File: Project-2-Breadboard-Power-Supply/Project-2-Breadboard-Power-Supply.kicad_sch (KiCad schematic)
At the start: 17 parts, among them J1 Conn_01x02_Pin, J2 Conn_01x02_Pin, J3 Conn_01x03_Pin, J4 Conn_01x03_Pin, J5 Screw_Terminal_01x02, J6 Barrel_Jack_Switch, J7 Screw_Terminal_01x02, U1 LM7805_TO220, U2 LM317_TO-220

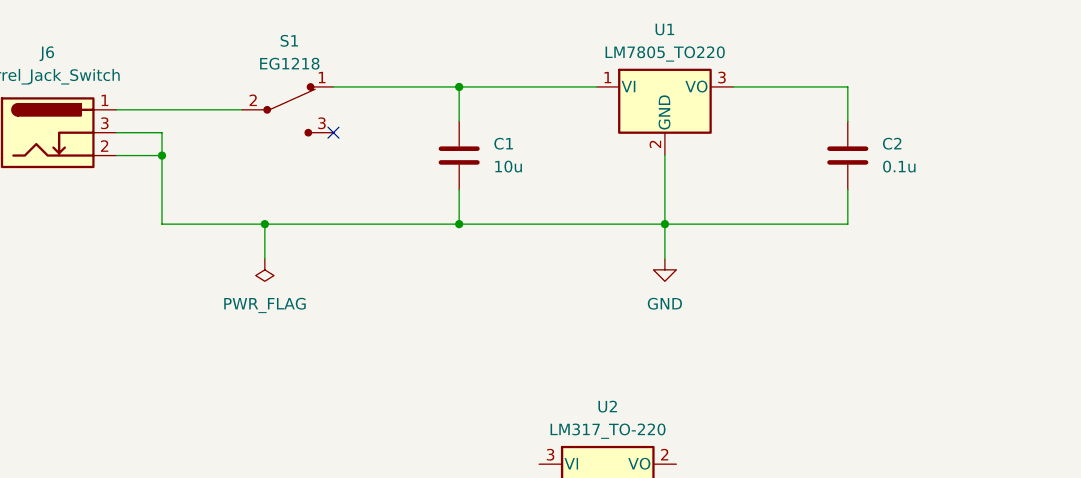
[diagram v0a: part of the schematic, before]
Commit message: add net names (step 5) for sub-net
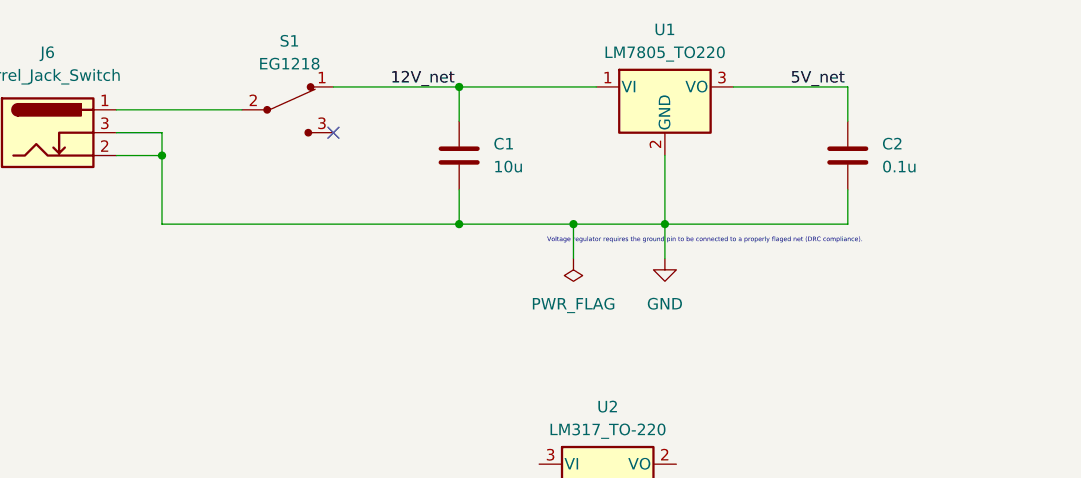
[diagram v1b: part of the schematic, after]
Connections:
- net 12V_net: now reaches C1.1, S1.1, U1.1 (VI)
- net 5V_net: now reaches C2.1, U1.3 (VO)
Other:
- note added: "Voltage regulator requires the ground pin to be connected to a properly flaged net (DRC compliance)."
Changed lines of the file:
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@@
 		(company "jupitersw.com")
+	)
+	(text "Voltage regulator requires the ground pin to be connected to a properly flaged net (DRC compliance)."
+		(exclude_from_sim no)
+		(at 111.125 52.705 0)
+		(effects
+			(font
+				(size 0.5 0.5)
+			)
+		)
 	)
 	(junction
@@
 	)
 	(junction
-		(at 62.23 50.8)
-		(diameter 0)
-		(color 0 0 0 0)
-	)
-	(junction
 		(at 83.82 35.56)
 		(diameter 0)
@@
 		(color 0 0 0 0)
 	)
+	(junction
+		(at 96.52 50.8)
+		(diameter 0)
+		(color 0 0 0 0)
+	)
 	(no_connect
 		(at 69.85 40.64)
@@
 	(wire
 		(pts
-			(xy 62.23 50.8) (xy 83.82 50.8)
-		)
-		(stroke
-			(width 0)
-			(type default)
-		)
-	)
-	(wire
-		(pts
 			(xy 45.72 43.18) (xy 50.8 43.18)
 		)
@@
 	(wire
 		(pts
-			(xy 62.23 50.8) (xy 62.23 54.61)
+			(xy 96.52 50.8) (xy 96.52 54.61)
 		)
 		(stroke
@@
 	(wire
 		(pts
-			(xy 50.8 50.8) (xy 62.23 50.8)
+			(xy 50.8 50.8) (xy 96.52 50.8)
 		)
 		(stroke
@@
 	(wire
 		(pts
-			(xy 83.82 50.8) (xy 106.68 50.8)
-		)
-		(stroke
-			(width 0)
-			(type default)
-		)
-	)
-	(wire
-		(pts
 			(xy 83.82 35.56) (xy 99.06 35.56)
 		)
@@
 	(wire
 		(pts
+			(xy 96.52 50.8) (xy 106.68 50.8)
+		)
+		(stroke
+			(width 0)
+			(type default)
+		)
+	)
+	(wire
+		(pts
 			(xy 50.8 40.64) (xy 50.8 43.18)
 		)
@@
 			(width 0)
 			(type default)
+		)
+	)
+	(label "5V_net"
+		(at 120.65 35.56 0)
+		(effects
+			(font
+				(size 1.27 1.27)
+			)
+			(justify left bottom)
+		)
+	)
+	(label "12V_net"
+		(at 76.2 35.56 0)
+		(effects
+			(font
+				(size 1.27 1.27)
+			)
+			(justify left bottom)
 		)
 	)
@@
 	(symbol
 		(lib_id "power:PWR_FLAG")
-		(at 62.23 54.61 180)
+		(at 96.52 54.61 180)
 		(unit 1)
 		(body_style 1)
@@
 		(fields_autoplaced yes)
 		(property "Reference" "#FLG01"
-			(at 62.23 56.515 0)
+			(at 96.52 56.515 0)
 			(hide yes)
 			(show_name no)
@@
 		)
 		(property "Value" "PWR_FLAG"
-			(at 62.23 59.69 0)
+			(at 96.52 59.69 0)
 			(show_name no)
 			(do_not_autoplace no)
@@
 		)
 		(property "Footprint" ""
-			(at 62.23 54.61 0)
+			(at 96.52 54.61 0)
 			(hide yes)
 			(show_name no)
@@
 		)
 		(property "Datasheet" ""
-			(at 62.23 54.61 0)
+			(at 96.52 54.61 0)
 			(hide yes)
 			(show_name no)
@@
 		)
 		(property "Description" "Special symbol for telling ERC where power comes from"
-			(at 62.23 54.61 0)
-			(hide yes)
-			(show_name no)
+			(at 96.52 54.61 0)
+			(hide yes)
+			(show_name no)

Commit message: add wiring, power flag, net labels to sub-circuit 2 (step 4, 5)
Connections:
- net 12V_net: now also R1.2, U2.3 (VI)
- net GND: now also C3.2, D1.1 (K), R3.1
- net at U2.1 (ADJ): now also R2.1, R3.2
- net 3.3V_net: now reaches U2.2 (VO)
- net 3.3V_net: now also C3.1, R2.2
- net at R1.1: now also D1.2 (A)
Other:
- moved on the sheet: D1, R1, R2, R3

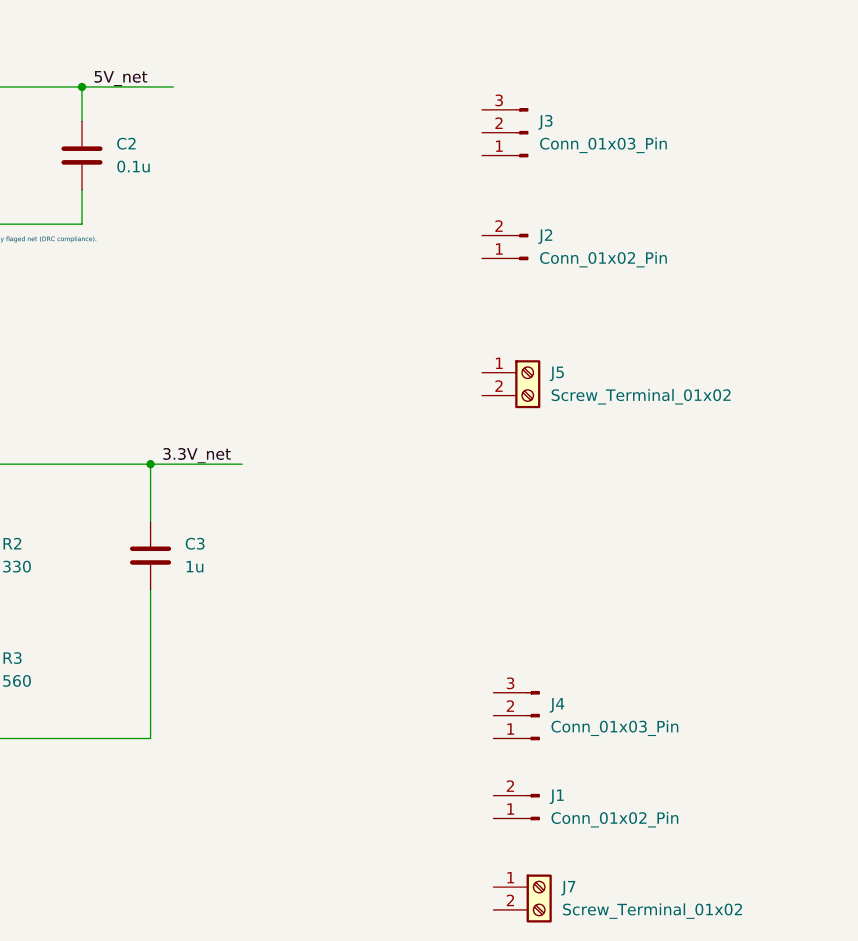
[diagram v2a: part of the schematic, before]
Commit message: add wiring, power flag, net labels to sub-circuits 3, 4 (step 4, 5)
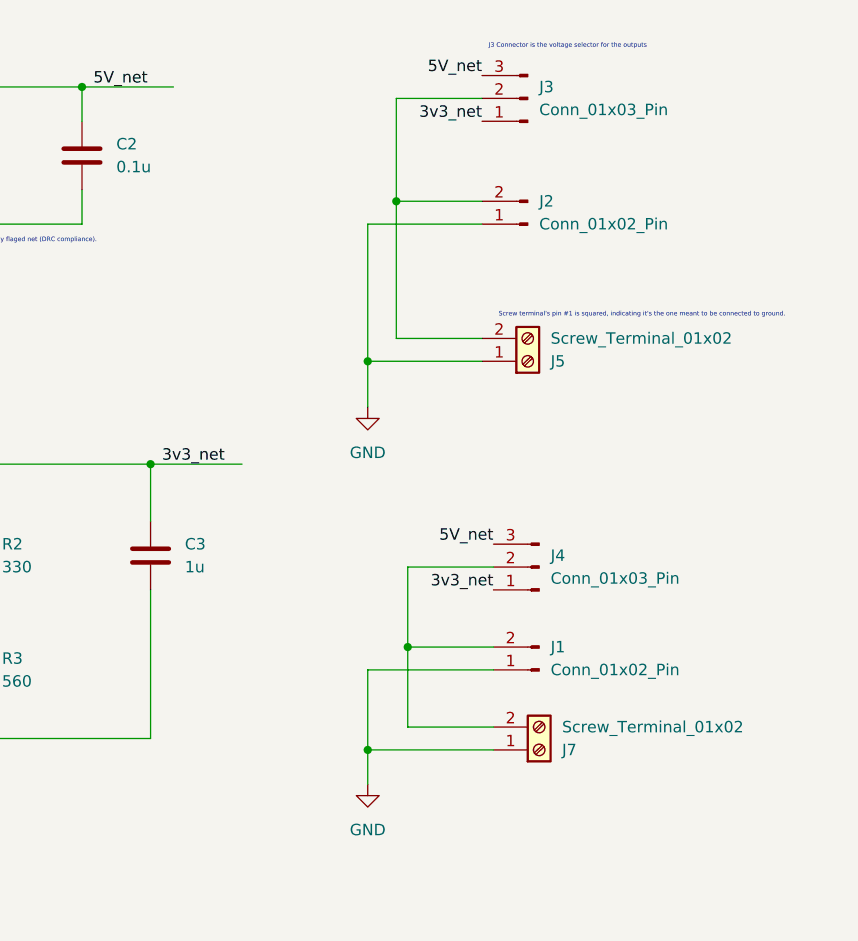
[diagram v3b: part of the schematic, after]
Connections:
- net 3.3V_net is gone; now on net 3v3_net: C3.1, R2.2, U2.2 (VO)
- net 5V_net: now also J3.3 (Pin_3), J4.3 (Pin_3)
- net GND: now also J1.1 (Pin_1), J2.1 (Pin_1), J5.1 (Pin_1), J7.1 (Pin_1)
- net 3v3_net: now reaches J4.1 (Pin_1)
- net 3v3_net: now also J3.1 (Pin_1)
- net at J4.2 (Pin_2): now also J1.2 (Pin_2), J7.2 (Pin_2)
- net at J2.2 (Pin_2): now also J3.2 (Pin_2), J5.2 (Pin_2)
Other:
- note added: "J3 Connector is the voltage selector for the outputs"
- note added: "Screw terminal's pin #1 is squared, indicating it's the one meant to be connected to ground."
- moved on the sheet: J1, J2, J3, J4, J5, J7

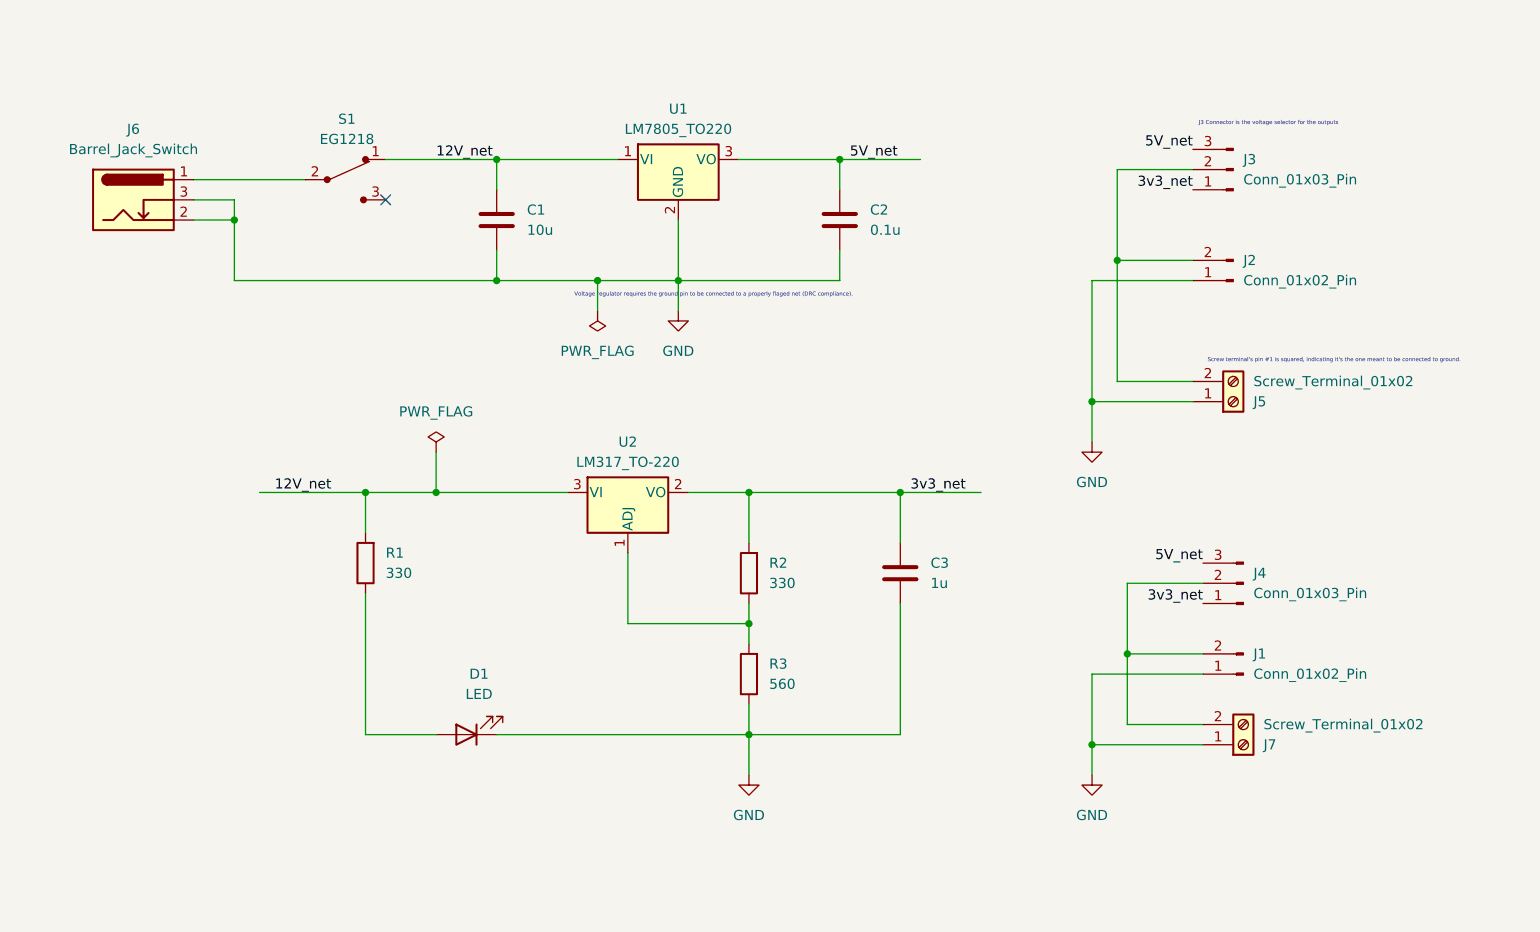
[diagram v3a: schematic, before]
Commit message: add nets labels, net classes (step 5)
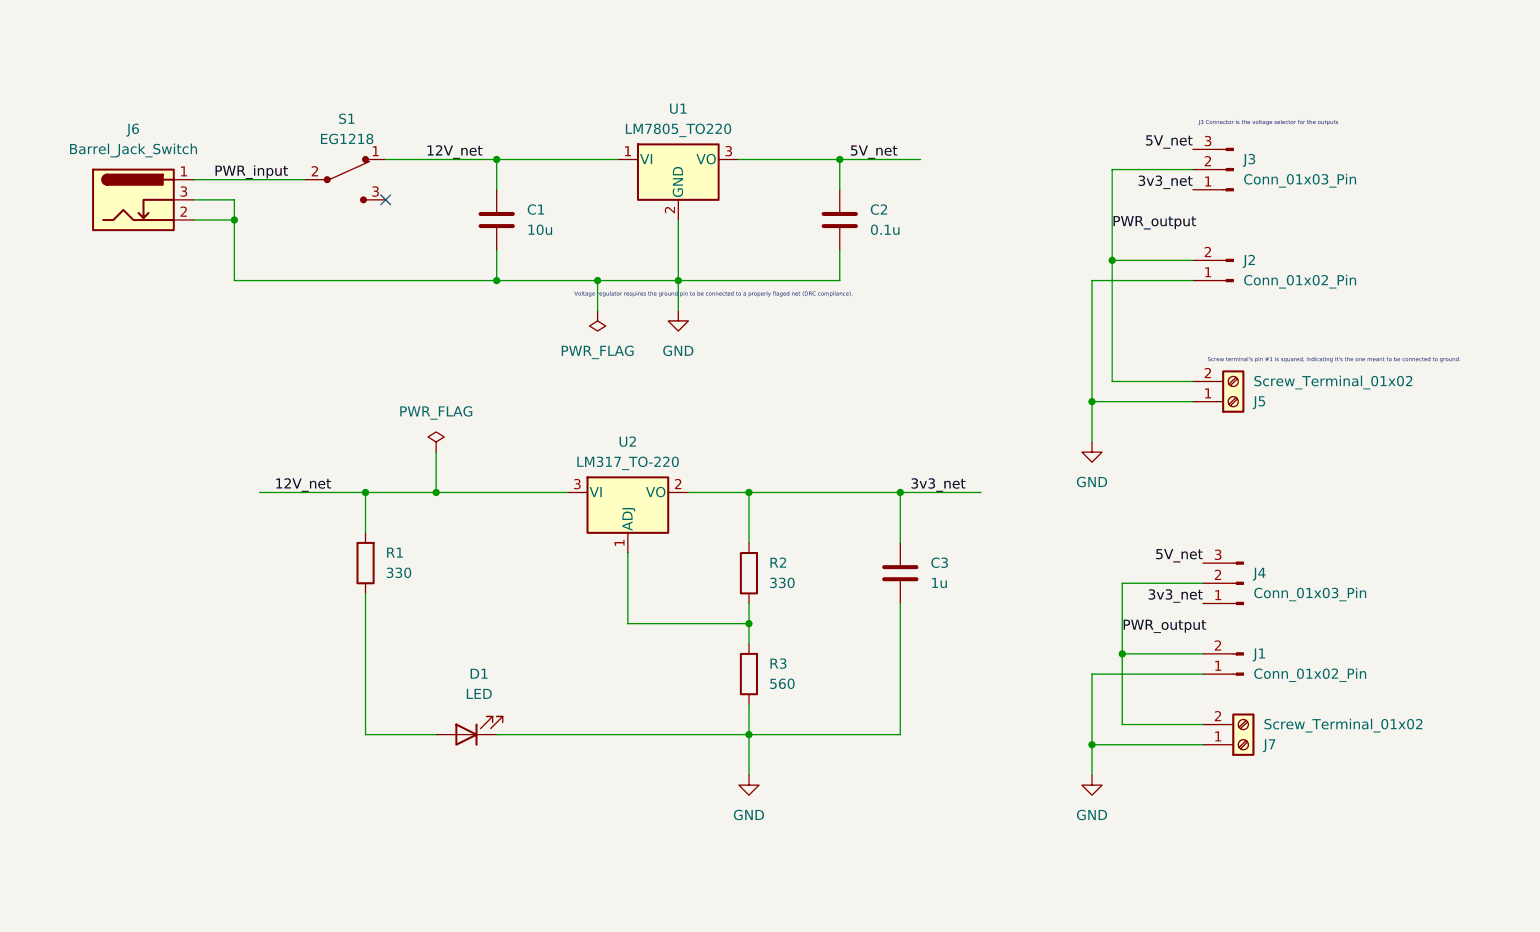
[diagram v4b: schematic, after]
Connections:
- net PWR_output: now reaches J1.2 (Pin_2), J4.2 (Pin_2), J7.2 (Pin_2)
- net PWR_output: now also J2.2 (Pin_2), J3.2 (Pin_2), J5.2 (Pin_2)
- net PWR_input: now reaches J6.1, S1.2
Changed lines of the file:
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@@
 	)
 	(junction
-		(at 163.195 97.79)
+		(at 162.56 97.79)
 		(diameter 0)
 		(color 0 0 0 0)
@@
 	)
 	(junction
-		(at 161.925 48.26)
-		(diameter 0)
-		(color 0 0 0 0)
-	)
-	(junction
 		(at 115.57 107.95)
 		(diameter 0)
@@
 	(junction
 		(at 83.82 50.8)
+		(diameter 0)
+		(color 0 0 0 0)
+	)
+	(junction
+		(at 161.29 48.26)
 		(diameter 0)
 		(color 0 0 0 0)
@@
 	(wire
 		(pts
-			(xy 161.925 63.5) (xy 171.45 63.5)
+			(xy 161.29 63.5) (xy 171.45 63.5)
 		)
 		(stroke
@@
 	(wire
 		(pts
+			(xy 161.29 48.26) (xy 171.45 48.26)
+		)
+		(stroke
+			(width 0)
+			(type default)
+		)
+	)
+	(wire
+		(pts
 			(xy 115.57 83.82) (xy 115.57 77.47)
 		)
@@
 	(wire
 		(pts
-			(xy 161.925 48.26) (xy 161.925 63.5)
+			(xy 161.29 48.26) (xy 161.29 63.5)
 		)
 		(stroke
@@
 	(wire
 		(pts
-			(xy 161.925 36.83) (xy 161.925 48.26)
+			(xy 161.29 36.83) (xy 161.29 48.26)
 		)
 		(stroke
@@
 	(wire
 		(pts
-			(xy 171.45 36.83) (xy 161.925 36.83)
+			(xy 171.45 36.83) (xy 161.29 36.83)
 		)
 		(stroke
@@
 	(wire
 		(pts
-			(xy 163.195 97.79) (xy 172.72 97.79)
-		)
-		(stroke
-			(width 0)
-			(type default)
-		)
-	)
-	(wire
-		(pts
-			(xy 161.925 48.26) (xy 171.45 48.26)
-		)
-		(stroke
-			(width 0)
-			(type default)
-		)
-	)
-	(wire
-		(pts
 			(xy 50.8 43.18) (xy 50.8 50.8)
 		)
@@
 	(wire
 		(pts
-			(xy 163.195 106.68) (xy 163.195 97.79)
+			(xy 162.56 106.68) (xy 162.56 97.79)
 		)
 		(stroke
@@
 	(wire
 		(pts
-			(xy 163.195 88.9) (xy 163.195 97.79)
+			(xy 162.56 88.9) (xy 162.56 97.79)
 		)
 		(stroke
@@
 	(wire
 		(pts
+			(xy 162.56 97.79) (xy 172.72 97.79)
+		)
+		(stroke
+			(width 0)
+			(type default)
+		)
+	)
+	(wire
+		(pts
 			(xy 158.75 50.8) (xy 158.75 66.04)
 		)
@@
 	(wire
 		(pts
-			(xy 172.72 106.68) (xy 163.195 106.68)
-		)
-		(stroke
-			(width 0)
-			(type default)
-		)
-	)
-	(wire
-		(pts
-			(xy 172.72 88.9) (xy 163.195 88.9)
+			(xy 172.72 106.68) (xy 162.56 106.68)
+		)
+		(stroke
+			(width 0)
+			(type default)
+		)
+	)
+	(wire
+		(pts
+			(xy 172.72 88.9) (xy 162.56 88.9)
 		)
 		(stroke
@@
 			(width 0)
 			(type default)
+		)
+	)
+	(label "12V_net"
+		(at 74.93 35.56 0)
+		(fields_autoplaced yes)
+		(effects
+			(font
+				(size 1.27 1.27)
+			)
+			(justify left bottom)
+		)
+		(property "Netclass" "power_input"
+			(at 74.93 36.83 0)
+			(hide yes)
+			(show_name no)
+			(do_not_autoplace no)
+			(effects
+				(font
+					(size 1.27 1.27)
+					(italic yes)
+				)
+				(justify left)
+			)
+		)
+	)
+	(label "PWR_output"
+		(at 161.29 44.45 0)
+		(fields_autoplaced yes)
+		(effects
+			(font
+				(size 1.27 1.27)
+			)
+			(justify left bottom)
+		)
+		(property "Netclass" "power_output"
+			(at 161.29 45.72 0)
+			(hide yes)
+			(show_name no)
+			(do_not_autoplace no)
+			(effects
+				(font
+					(size 1.27 1.27)
+					(italic yes)
+				)
+				(justify left)
+			)
 		)
 	)
 	(label "3v3_net"
 		(at 135.89 77.47 0)
+		(fields_autoplaced yes)
 		(effects
 			(font
@@
 			(justify left bottom)
 		)
-	)
-	(label "12V_net"
-		(at 76.2 35.56 0)
-		(effects
-			(font
-				(size 1.27 1.27)
-			)
-			(justify left bottom)
+		(property "Netclass" "power_output"
+			(at 135.89 78.74 0)
+			(hide yes)
+			(show_name no)
+			(do_not_autoplace no)
+			(effects
+				(font
+					(size 1.27 1.27)
+					(italic yes)
+				)
+				(justify left)
+			)
 		)
 	)
 	(label "3v3_net"
 		(at 172.72 91.44 180)
+		(fields_autoplaced yes)
 		(effects
 			(font
@@
 			)
 			(justify right bottom)
+		)
+		(property "Netclass" "power_output"
+			(at 172.72 92.71 0)
+			(hide yes)
+			(show_name no)
+			(do_not_autoplace no)
+			(effects
+				(font
+					(size 1.27 1.27)
+					(italic yes)
+				)
+				(justify right)
+			)
 		)
 	)
@@
 			(justify right bottom)
 		)
+		(property "Netclass" "power_output"
+			(at 171.45 39.37 0)
+			(hide yes)
+			(show_name no)
+			(do_not_autoplace no)
+			(effects
+				(font
+					(size 1.27 1.27)
+					(italic yes)
+				)
+			)
+		)
+	)
+	(label "PWR_input"
+		(at 48.26 38.1 0)
+		(fields_autoplaced yes)
+		(effects
+			(font
+				(size 1.27 1.27)
+			)
+			(justify left bottom)
+		)
+		(property "Netclass" "power_input"
+			(at 48.26 39.37 0)
+			(hide yes)
+			(show_name no)
+			(do_not_autoplace no)
+			(effects
+				(font
+					(size 1.27 1.27)
+					(italic yes)
+				)
+				(justify left)
+			)
+		)
 	)
 	(label "5V_net"
 		(at 172.72 86.36 180)
+		(fields_autoplaced yes)
 		(effects
 			(font
@@
 			)
 			(justify right bottom)
+		)
+		(property "Netclass" "power_output"
+			(at 172.72 87.63 0)
+			(hide yes)
+			(show_name no)
+			(do_not_autoplace no)
+			(effects
+				(font
+					(size 1.27 1.27)
+					(italic yes)
+				)
+				(justify right)
+			)
 		)
 	)
 	(label "12V_net"
 		(at 55.88 77.47 0)
+		(fields_autoplaced yes)
 		(effects
 			(font
@@
 			)
 			(justify left bottom)
+		)
+		(property "Netclass" "power_input"
+			(at 55.88 78.74 0)
+			(hide yes)
+			(show_name no)
+			(do_not_autoplace no)
+			(effects
+				(font
+					(size 1.27 1.27)
+					(italic yes)
+				)
+				(justify left)
+			)
 		)
 	)
 	(label "5V_net"
 		(at 171.45 34.29 180)
+		(fields_autoplaced yes)
 		(effects
 			(font
@@
 			)
 			(justify right bottom)
+		)
+		(property "Netclass" "power_output"
+			(at 171.45 35.56 0)
+			(hide yes)
+			(show_name no)
+			(do_not_autoplace no)
+			(effects
+				(font
+					(size 1.27 1.27)
+					(italic yes)
+				)
+				(justify right)
+			)
+		)
+	)
+	(label "PWR_output"
+		(at 162.56 95.25 0)
+		(fields_autoplaced yes)
+		(effects
+			(font
+				(size 1.27 1.27)
+			)
+			(justify left bottom)
+		)
+		(property "Netclass" "power_output"
+			(at 162.56 96.52 0)
+			(hide yes)
+			(show_name no)
+			(do_not_autoplace no)
+			(effects
+				(font
+					(size 1.27 1.27)
+					(italic yes)
+				)
+				(justify left)
+			)
 		)
 	)
@@
 			(justify left bottom)
 		)
-	)
+		(property "Netclass" "power_output"
+			(at 128.27 35.56 0)
+			(hide yes)
+			(show_name no)
+			(do_not_autoplace no)
+			(effects
+				(font
+					(size 1.27 1.27)
+					(italic yes)
+				)
+			)
+		)
+	)
